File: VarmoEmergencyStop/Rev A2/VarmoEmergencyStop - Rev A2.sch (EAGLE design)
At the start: 7 parts, among them X1 NC3MAV, X2 NC3FAV2, X3 NC3MAV

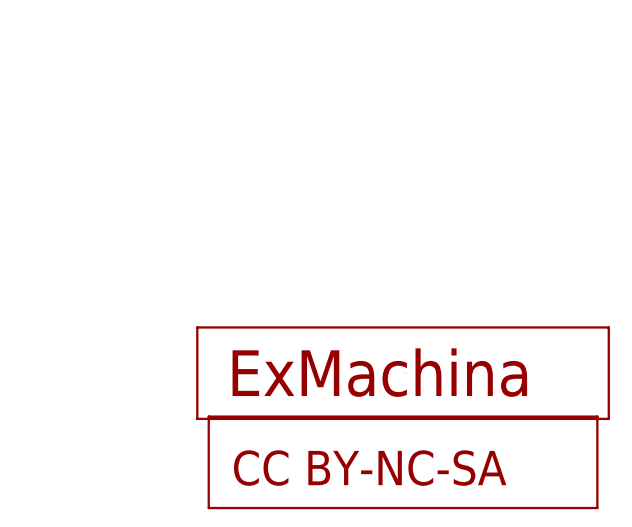
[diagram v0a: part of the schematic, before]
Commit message: Update VarmoEmergencyStop - Rev A2
* Add ExMachina logo to the back of the board
* Resize the board to the minimal
* Fix clearance issue
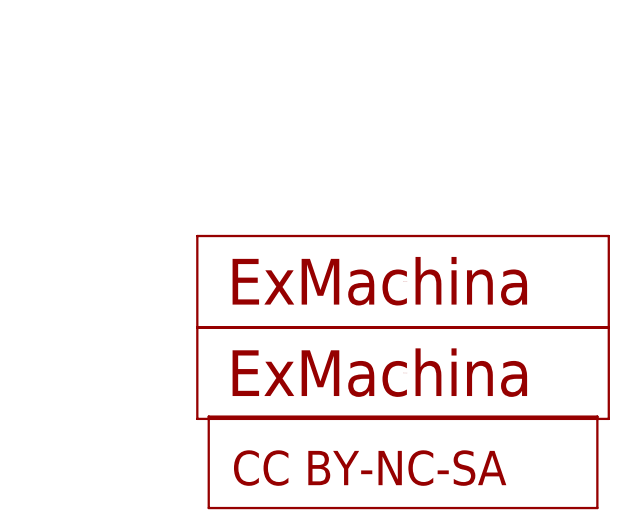
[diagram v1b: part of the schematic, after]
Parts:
- added U$3: EXMACHINA-LOGO-NAME, exmachina:EXMACHINA-LOGO-NAME
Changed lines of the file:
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@@
 <part name="GND3" library="supply1" deviceset="GND" device=""/>
 <part name="LED" library="con-molex" deviceset="22-?-03" device="05-7038"/>
+<part name="U$3" library="exmachina" deviceset="EXMACHINA-LOGO" device="-NAME"/>
 </parts>
 <sheets>
@@
 <instance part="LED" gate="-2" x="114.3" y="182.88" rot="R90"/>
 <instance part="LED" gate="-3" x="116.84" y="182.88" rot="R90"/>
+<instance part="U$3" gate="G$1" x="315.468" y="28.956"/>
 </instances>
 <busses>
